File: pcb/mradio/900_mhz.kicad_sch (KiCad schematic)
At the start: 5 parts, among them J401 MM60-52B1-E1-R650

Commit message: some fixes, missing level shifter
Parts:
- added R402: 10k, symbol Device:R
- added TP1, TP2, TP3, TP4, TP5: TestPoint, symbol Connector:TestPoint
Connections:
- net +3V3: now also R401.2, R402.1
- net GND: no longer R401.2
- net SPI1_CS: now also R402.2, TP4.1
- net SPI1_MISO: now also TP2.1
- net SPI1_MOSI: now also TP3.1
- net SPI1_SCK: now also TP1.1
- net SPI_INT: now also TP5.1
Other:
- moved on the sheet: R401

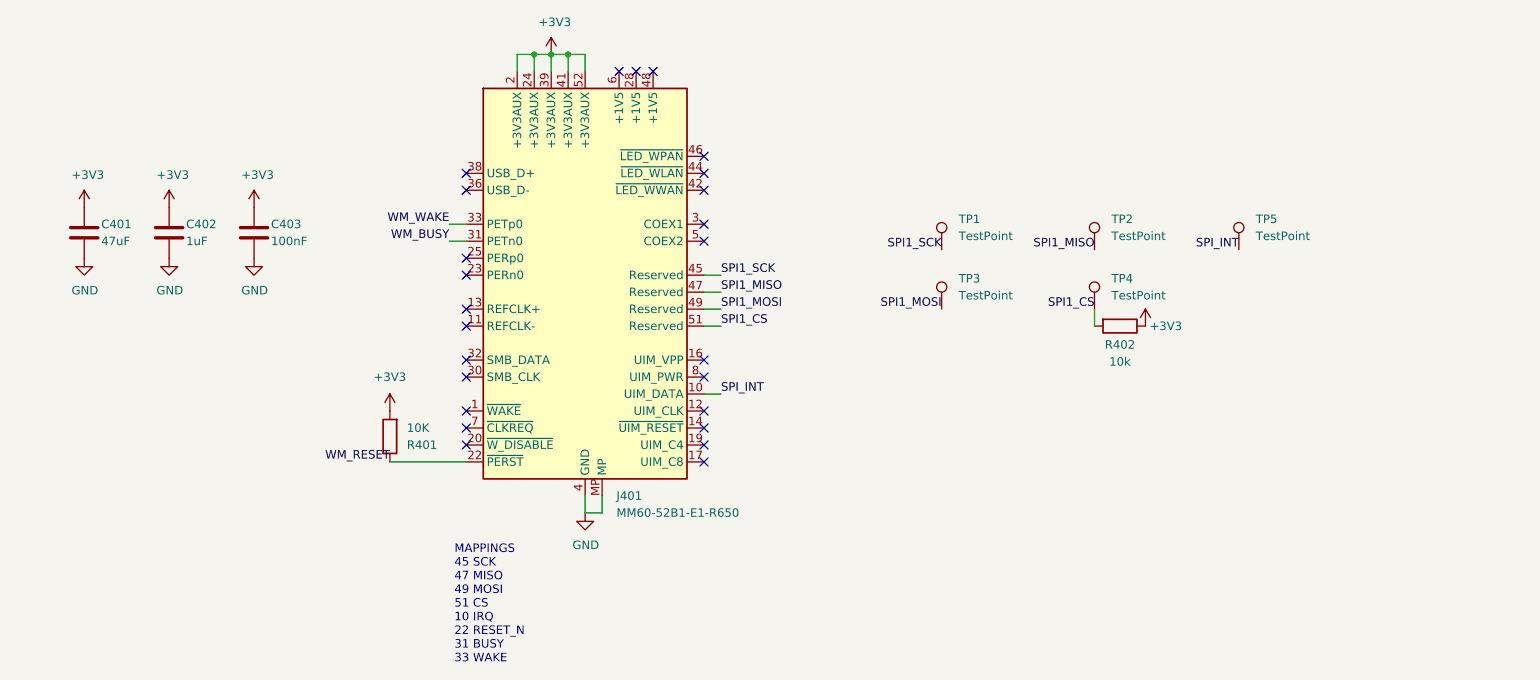
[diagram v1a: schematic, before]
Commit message: level shifters and necessary pull up/downs for 900mhz, kicad autofixes
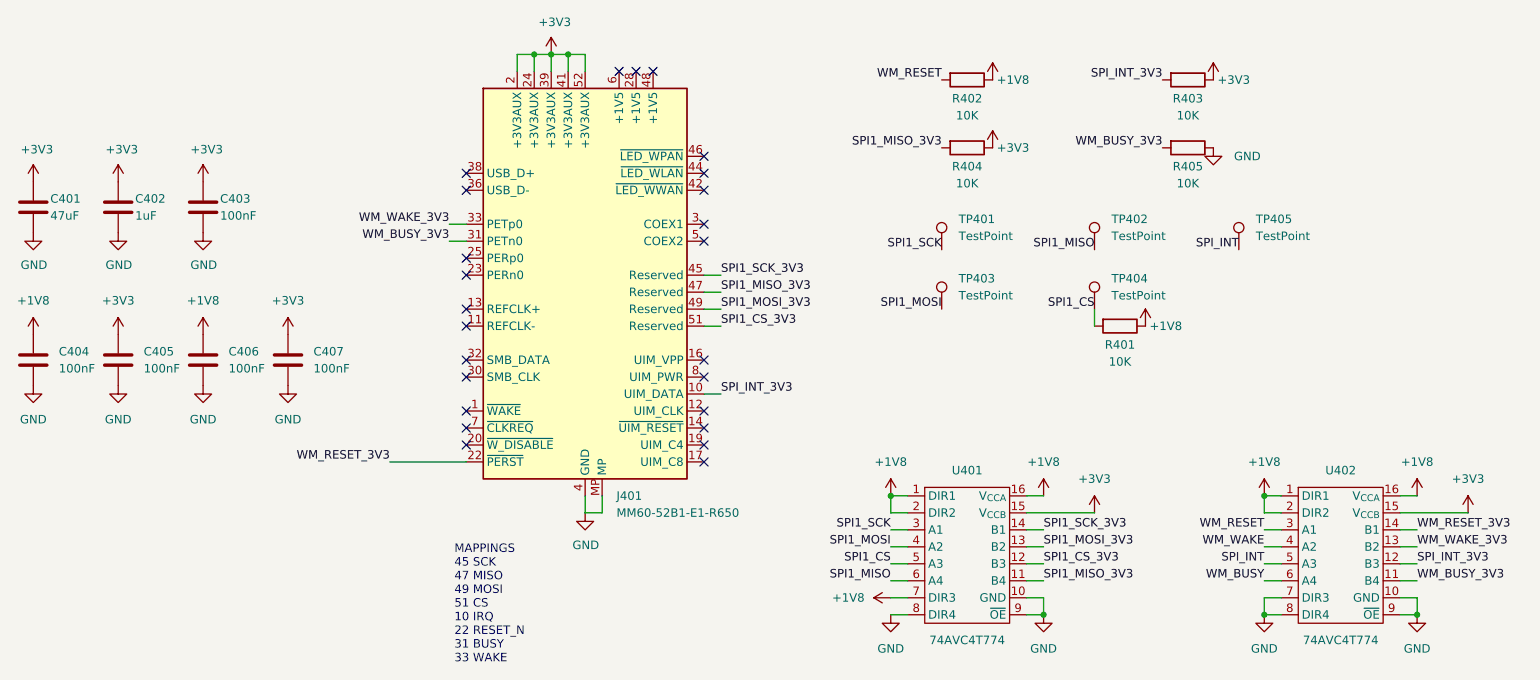
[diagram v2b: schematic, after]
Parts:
- removed R401: 10K, Resistor_SMD:R_0603_1608Metric, symbol Device:R
- added C404, C405, C406, C407: 100nF, Capacitor_SMD:C_0603_1608Metric, symbol Device:C
- added R402, R403, R404, R405: 10K, Resistor_SMD:R_0603_1608Metric, symbol Device:R
- added U401, U402: 74AVC4T774, Package_SO:TSSOP-16_4.4x5mm_P0.65mm, symbol 74AVC4T774QPWRQ1:74AVC4T774QPWRQ1
- R401: renamed from R402; value 10k -> 10K; footprint (none) -> Resistor_SMD:R_0603_1608Metric
- TP401: renamed from TP1; footprint (none) -> TestPoint:TestPoint_Pad_D1.0mm
- TP402: renamed from TP2; footprint (none) -> TestPoint:TestPoint_Pad_D1.0mm
- TP403: renamed from TP3; footprint (none) -> TestPoint:TestPoint_Pad_D1.0mm
- TP404: renamed from TP4; footprint (none) -> TestPoint:TestPoint_Pad_D1.0mm
- TP405: renamed from TP5; footprint (none) -> TestPoint:TestPoint_Pad_D1.0mm
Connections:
- net +3V3: now also C405.1, C407.1, R403.1, R404.1, U401.15 (V_{CCB}), U402.15 (V_{CCB}); no longer R401.1
- net GND: now also C404.2, C405.2, C406.2, C407.2, R405.1, U401.10 (GND), U401.8 (DIR4), U401.9 (~{OE}), U402.10 (GND), U402.7 (DIR3), U402.8 (DIR4), U402.9 (~{OE})
- net SPI1_CS: now also U401.5 (A3); no longer J401.51 (Reserved)
- net SPI1_MISO: now also U401.6 (A4); no longer J401.47 (Reserved)
- net SPI1_MOSI: now also U401.4 (A2); no longer J401.49 (Reserved)
- net SPI1_SCK: now also U401.3 (A1); no longer J401.45 (Reserved)
- net SPI_INT: now also U402.5 (A3); no longer J401.10 (UIM_DATA)
- net WM_BUSY: now also U402.6 (A4); no longer J401.31 (PETn0)
- net WM_RESET: now also R402.2, U402.3 (A1); no longer J401.22 (~{PERST})
- net WM_WAKE: now also U402.4 (A2); no longer J401.33 (PETp0)
- new net +1V8: C404.1, C406.1, R401.1, R402.1, U401.1 (DIR1), U401.16 (V_{CCA}), U401.2 (DIR2), U401.7 (DIR3), U402.1 (DIR1), U402.16 (V_{CCA}), U402.2 (DIR2)
- new net SPI1_CS_3V3: J401.51 (Reserved), U401.12 (B3)
- new net SPI1_MISO_3V3: J401.47 (Reserved), R404.2, U401.11 (B4)
- new net SPI1_MOSI_3V3: J401.49 (Reserved), U401.13 (B2)
- new net SPI1_SCK_3V3: J401.45 (Reserved), U401.14 (B1)
- new net SPI_INT_3V3: J401.10 (UIM_DATA), R403.2, U402.12 (B3)
- new net WM_BUSY_3V3: J401.31 (PETn0), R405.2, U402.11 (B4)
- new net WM_RESET_3V3: J401.22 (~{PERST}), U402.14 (B1)
- new net WM_WAKE_3V3: J401.33 (PETp0), U402.13 (B2)
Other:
- moved on the sheet: C401, C402, C403

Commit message: Fixed numbers
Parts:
- removed C404, C405, C406, C407: 100nF, Capacitor_SMD:C_0603_1608Metric, symbol Device:C
- removed R402, R403, R404, R405: 10K, Resistor_SMD:R_0603_1608Metric, symbol Device:R
- removed U401, U402: 74AVC4T774, Package_SO:TSSOP-16_4.4x5mm_P0.65mm, symbol 74AVC4T774QPWRQ1:74AVC4T774QPWRQ1
- added R401: 10K, Resistor_SMD:R_0603_1608Metric, symbol Device:R
- R402: renamed from R401; value 10K -> 10k; footprint Resistor_SMD:R_0603_1608Metric -> (none)
- TP401, TP404, TP405: footprint TestPoint:TestPoint_Pad_D1.0mm -> (none)
- TP402: renamed from TP403; footprint TestPoint:TestPoint_Pad_D1.0mm -> (none)
- TP403: renamed from TP402; footprint TestPoint:TestPoint_Pad_D1.0mm -> (none)
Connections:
- net +1V8 is gone; now on net +3V3: R402.1
- net SPI1_CS_3V3 is gone; now on net SPI1_CS: J401.51 (Reserved)
- net SPI1_MISO_3V3 is gone; now on net SPI1_MISO: J401.47 (Reserved)
- net SPI1_MOSI_3V3 is gone; now on net SPI1_MOSI: J401.49 (Reserved)
- net SPI1_SCK_3V3 is gone; now on net SPI1_SCK: J401.45 (Reserved)
- net SPI_INT_3V3 is gone; now on net SPI_INT: J401.10 (UIM_DATA)
- net WM_BUSY_3V3 is gone; now on net WM_BUSY: J401.31 (PETn0)
- net WM_RESET_3V3 is gone; now on net WM_RESET: J401.22 (~{PERST})
- net WM_WAKE_3V3 is gone; now on net WM_WAKE: J401.33 (PETp0)
- net +3V3: now also R401.2
- net WM_RESET: now also R401.1
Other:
- moved on the sheet: C401, C402, C403

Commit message: undid overwrite
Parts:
- removed R401: 10K, Resistor_SMD:R_0603_1608Metric, symbol Device:R
- added C404, C405, C406, C407: 100nF, Capacitor_SMD:C_0603_1608Metric, symbol Device:C
- added R402, R403, R404, R405: 10K, Resistor_SMD:R_0603_1608Metric, symbol Device:R
- added U401, U402: 74AVC4T774, Package_SO:TSSOP-16_4.4x5mm_P0.65mm, symbol 74AVC4T774QPWRQ1:74AVC4T774QPWRQ1
- R401: renamed from R402; value 10k -> 10K; footprint (none) -> Resistor_SMD:R_0603_1608Metric
- TP401, TP404, TP405: footprint (none) -> TestPoint:TestPoint_Pad_D1.0mm
- TP402: renamed from TP403; footprint (none) -> TestPoint:TestPoint_Pad_D1.0mm
- TP403: renamed from TP402; footprint (none) -> TestPoint:TestPoint_Pad_D1.0mm
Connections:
- net +3V3: now also C405.1, C407.1, R403.1, R404.1, U401.15 (V_{CCB}), U402.15 (V_{CCB}); no longer R401.1
- net GND: now also C404.2, C405.2, C406.2, C407.2, R405.1, U401.10 (GND), U401.8 (DIR4), U401.9 (~{OE}), U402.10 (GND), U402.7 (DIR3), U402.8 (DIR4), U402.9 (~{OE})
- net SPI1_CS: now also U401.5 (A3); no longer J401.51 (Reserved)
- net SPI1_MISO: now also U401.6 (A4); no longer J401.47 (Reserved)
- net SPI1_MOSI: now also U401.4 (A2); no longer J401.49 (Reserved)
- net SPI1_SCK: now also U401.3 (A1); no longer J401.45 (Reserved)
- net SPI_INT: now also U402.5 (A3); no longer J401.10 (UIM_DATA)
- net WM_BUSY: now also U402.6 (A4); no longer J401.31 (PETn0)
- net WM_RESET: now also R402.2, U402.3 (A1); no longer J401.22 (~{PERST})
- net WM_WAKE: now also U402.4 (A2); no longer J401.33 (PETp0)
- new net +1V8: C404.1, C406.1, R401.1, R402.1, U401.1 (DIR1), U401.16 (V_{CCA}), U401.2 (DIR2), U401.7 (DIR3), U402.1 (DIR1), U402.16 (V_{CCA}), U402.2 (DIR2)
- new net SPI1_CS_3V3: J401.51 (Reserved), U401.12 (B3)
- new net SPI1_MISO_3V3: J401.47 (Reserved), R404.2, U401.11 (B4)
- new net SPI1_MOSI_3V3: J401.49 (Reserved), U401.13 (B2)
- new net SPI1_SCK_3V3: J401.45 (Reserved), U401.14 (B1)
- new net SPI_INT_3V3: J401.10 (UIM_DATA), R403.2, U402.12 (B3)
- new net WM_BUSY_3V3: J401.31 (PETn0), R405.2, U402.11 (B4)
- new net WM_RESET_3V3: J401.22 (~{PERST}), U402.14 (B1)
- new net WM_WAKE_3V3: J401.33 (PETp0), U402.13 (B2)
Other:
- moved on the sheet: C401, C402, C403
